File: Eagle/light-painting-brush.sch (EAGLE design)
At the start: 24 parts, among them IC1 TPS61070DDC, T1 2N3904, T2 2N3904, T3 2N3904

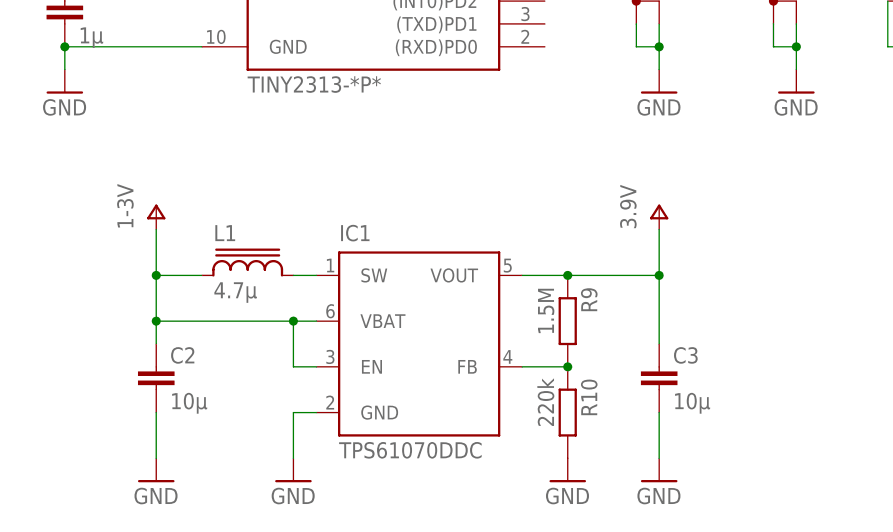
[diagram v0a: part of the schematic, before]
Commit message: Remove TPS61070 boost converter
Previous version of the board is saved in the "tps61070" branch.
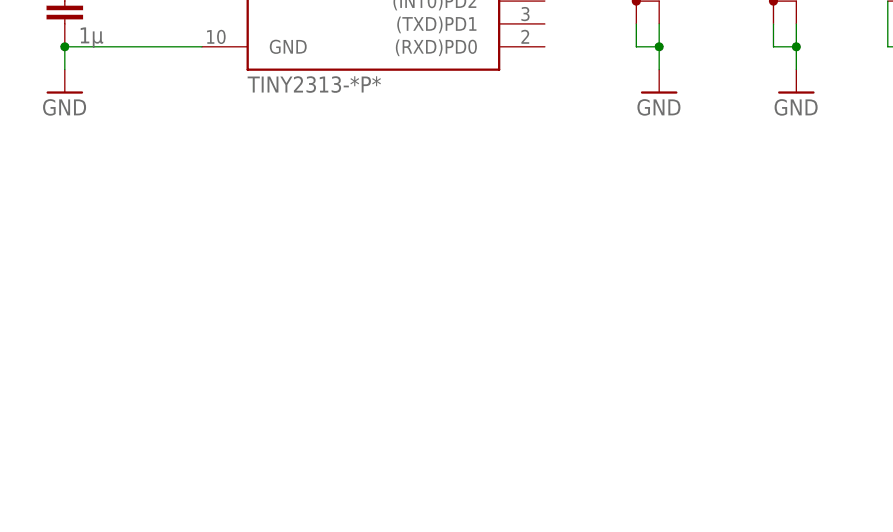
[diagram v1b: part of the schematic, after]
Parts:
- removed C2, C3: 10μ, rcl:C-EUC1206
- removed IC1: TPS61070DDC, Gumix:TPS61070DDC
- removed L1: 4.7μ, inductor-sumida:CR43
- removed R10: 220k, resistor:R-EU_R1206
- removed R9: 1.5M, resistor:R-EU_R1206
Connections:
- removed net N$13: IC1.SW, L1.2
- removed net N$14: IC1.FB, R10.1, R9.2
- net GND: no longer C2.2, C3.2, IC1.GND, R10.2
- net V+: no longer C2.1, C3.1, IC1.EN, IC1.VBAT, IC1.VOUT, L1.1, R9.1
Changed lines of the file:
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@@
 <part name="R2" library="resistor" deviceset="R-EU_" device="R1206" value="10k"/>
 <part name="R3" library="resistor" deviceset="R-EU_" device="R1206" value="10k"/>
-<part name="3V" library="supply1" deviceset="V+" device="" value="1-3V"/>
 <part name="4V" library="supply1" deviceset="V+" device="" value="3.9V"/>
 <part name="T1" library="transistor" deviceset="2N3904" device=""/>
@@
 <part name="4V2" library="supply1" deviceset="V+" device="" value="3.9V"/>
 <part name="4V3" library="supply1" deviceset="V+" device="" value="3.9V"/>
-<part name="L1" library="inductor-sumida" deviceset="CR43" device="" value="4.7μ"/>
-<part name="GND2" library="supply1" deviceset="GND" device=""/>
-<part name="IC1" library="Gumix" deviceset="TPS6107*" device="DDC" technology="0"/>
-<part name="4V4" library="supply1" deviceset="V+" device="" value="3.9V"/>
-<part name="R9" library="resistor" deviceset="R-EU_" device="R1206" value="1.5M"/>
-<part name="R10" library="resistor" deviceset="R-EU_" device="R1206" value="220k"/>
-<part name="GND5" library="supply1" deviceset="GND" device=""/>
-<part name="C2" library="rcl" deviceset="C-EU" device="C1206" value="10μ"/>
-<part name="C3" library="rcl" deviceset="C-EU" device="C1206" value="10μ"/>
-<part name="GND6" library="supply1" deviceset="GND" device=""/>
-<part name="GND7" library="supply1" deviceset="GND" device=""/>
 <part name="GND8" library="supply1" deviceset="GND" device=""/>
 <part name="GND9" library="supply1" deviceset="GND" device=""/>
@@
 <attribute name="VALUE" x="29.718" y="59.69" size="1.778" layer="96" rot="R270"/>
 </instance>
-<instance part="3V" gate="1" x="-38.1" y="-5.08" smashed="yes">
-<attribute name="VALUE" x="-40.64" y="-7.62" size="1.778" layer="96" rot="R90"/>
-</instance>
 <instance part="4V" gate="1" x="-48.26" y="66.04" smashed="yes">
 <attribute name="VALUE" x="-50.8" y="63.5" size="1.778" layer="96" rot="R90"/>
@@
 <instance part="4V3" gate="1" x="86.36" y="66.04" smashed="yes">
 <attribute name="VALUE" x="83.82" y="63.5" size="1.778" layer="96" rot="R90"/>
-</instance>
-<instance part="L1" gate="G$1" x="-27.94" y="-12.7" smashed="yes">
-<attribute name="NAME" x="-31.75" y="-8.89" size="1.778" layer="95"/>
-<attribute name="VALUE" x="-31.75" y="-15.24" size="1.778" layer="96"/>
-</instance>
-<instance part="GND2" gate="1" x="-38.1" y="-35.56" smashed="yes">
-<attribute name="VALUE" x="-40.64" y="-38.1" size="1.778" layer="96"/>
-</instance>
-<instance part="IC1" gate="G$1" x="-10.16" y="-20.32" smashed="yes">
-<attribute name="NAME" x="-17.78" y="-8.89" size="1.778" layer="95"/>
-<attribute name="VALUE" x="-17.78" y="-33.02" size="1.778" layer="96"/>
-</instance>
-<instance part="4V4" gate="1" x="17.78" y="-5.08" smashed="yes">
-<attribute name="VALUE" x="15.24" y="-7.62" size="1.778" layer="96" rot="R90"/>
-</instance>
-<instance part="R9" gate="G$1" x="7.62" y="-17.78" smashed="yes" rot="R270">
-<attribute name="NAME" x="9.1186" y="-13.97" size="1.778" layer="95" rot="R270"/>
-<attribute name="VALUE" x="4.318" y="-13.97" size="1.778" layer="96" rot="R270"/>
-</instance>
-<instance part="R10" gate="G$1" x="7.62" y="-27.94" smashed="yes" rot="R270">
-<attribute name="NAME" x="9.1186" y="-24.13" size="1.778" layer="95" rot="R270"/>
-<attribute name="VALUE" x="4.318" y="-24.13" size="1.778" layer="96" rot="R270"/>
-</instance>
-<instance part="GND5" gate="1" x="7.62" y="-35.56" smashed="yes">
-<attribute name="VALUE" x="5.08" y="-38.1" size="1.778" layer="96"/>
-</instance>
-<instance part="C2" gate="G$1" x="-38.1" y="-22.86" smashed="yes">
-<attribute name="NAME" x="-36.576" y="-22.479" size="1.778" layer="95"/>
-<attribute name="VALUE" x="-36.576" y="-27.559" size="1.778" layer="96"/>
-</instance>
-<instance part="C3" gate="G$1" x="17.78" y="-22.86" smashed="yes">
-<attribute name="NAME" x="19.304" y="-22.479" size="1.778" layer="95"/>
-<attribute name="VALUE" x="19.304" y="-27.559" size="1.778" layer="96"/>
-</instance>
-<instance part="GND6" gate="1" x="-22.86" y="-35.56" smashed="yes">
-<attribute name="VALUE" x="-25.4" y="-38.1" size="1.778" layer="96"/>
-</instance>
-<instance part="GND7" gate="1" x="17.78" y="-35.56" smashed="yes">
-<attribute name="VALUE" x="15.24" y="-38.1" size="1.778" layer="96"/>
 </instance>
 <instance part="GND8" gate="1" x="17.78" y="7.62" smashed="yes">
@@
 <pinref part="GND3" gate="1" pin="GND"/>
 <wire x1="50.8" y1="0" x2="50.8" y2="-2.54" width="0.1524" layer="91"/>
-</segment>
-<segment>
-<pinref part="R10" gate="G$1" pin="2"/>
-<pinref part="GND5" gate="1" pin="GND"/>
-</segment>
-<segment>
-<pinref part="GND6" gate="1" pin="GND"/>
-<wire x1="-22.86" y1="-33.02" x2="-22.86" y2="-27.94" width="0.1524" layer="91"/>
-<pinref part="IC1" gate="G$1" pin="GND"/>
-<wire x1="-22.86" y1="-27.94" x2="-20.32" y2="-27.94" width="0.1524" layer="91"/>
-</segment>
-<segment>
-<pinref part="C2" gate="G$1" pin="2"/>
-<pinref part="GND2" gate="1" pin="GND"/>
-<wire x1="-38.1" y1="-27.94" x2="-38.1" y2="-33.02" width="0.1524" layer="91"/>
-</segment>
-<segment>
-<pinref part="GND7" gate="1" pin="GND"/>
-<pinref part="C3" gate="G$1" pin="2"/>
-<wire x1="17.78" y1="-33.02" x2="17.78" y2="-27.94" width="0.1524" layer="91"/>
 </segment>
 <segment>
@@
 </segment>
 <segment>
-<pinref part="3V" gate="1" pin="V+"/>
-<wire x1="-38.1" y1="-7.62" x2="-38.1" y2="-12.7" width="0.1524" layer="91"/>
-<pinref part="L1" gate="G$1" pin="1"/>
-<wire x1="-38.1" y1="-12.7" x2="-33.02" y2="-12.7" width="0.1524" layer="91"/>
-<wire x1="-38.1" y1="-20.32" x2="-38.1" y2="-17.78" width="0.1524" layer="91"/>
-<junction x="-38.1" y="-12.7"/>
-<pinref part="C2" gate="G$1" pin="1"/>
-<pinref part="IC1" gate="G$1" pin="VBAT"/>
-<wire x1="-38.1" y1="-17.78" x2="-38.1" y2="-12.7" width="0.1524" layer="91"/>
-<wire x1="-20.32" y1="-17.78" x2="-22.86" y2="-17.78" width="0.1524" layer="91"/>
-<pinref part="IC1" gate="G$1" pin="EN"/>
-<wire x1="-20.32" y1="-22.86" x2="-22.86" y2="-22.86" width="0.1524" layer="91"/>
-<wire x1="-22.86" y1="-22.86" x2="-22.86" y2="-17.78" width="0.1524" layer="91"/>
-<wire x1="-22.86" y1="-17.78" x2="-38.1" y2="-17.78" width="0.1524" layer="91"/>
-<junction x="-38.1" y="-17.78"/>
-<junction x="-22.86" y="-17.78"/>
-</segment>
-<segment>
-<pinref part="IC1" gate="G$1" pin="VOUT"/>
-<wire x1="2.54" y1="-12.7" x2="7.62" y2="-12.7" width="0.1524" layer="91"/>
-<pinref part="R9" gate="G$1" pin="1"/>
-<junction x="7.62" y="-12.7"/>
-<pinref part="4V4" gate="1" pin="V+"/>
-<wire x1="7.62" y1="-12.7" x2="17.78" y2="-12.7" width="0.1524" layer="91"/>
-<wire x1="17.78" y1="-12.7" x2="17.78" y2="-7.62" width="0.1524" layer="91"/>
-<pinref part="C3" gate="G$1" pin="1"/>
-<wire x1="17.78" y1="-20.32" x2="17.78" y2="-12.7" width="0.1524" layer="91"/>
-<junction x="17.78" y="-12.7"/>
-</segment>
-<segment>
 <pinref part="R2" gate="G$1" pin="1"/>
 <pinref part="4V5" gate="1" pin="V+"/>
@@
 </segment>
 </net>
-<net name="N$13" class="0">
-<segment>
-<pinref part="L1" gate="G$1" pin="2"/>
-<wire x1="-20.32" y1="-12.7" x2="-22.86" y2="-12.7" width="0.1524" layer="91"/>
-<pinref part="IC1" gate="G$1" pin="SW"/>
-</segment>
-</net>
-<net name="N$14" class="0">
-<segment>
-<pinref part="R9" gate="G$1" pin="2"/>
-<pinref part="R10" gate="G$1" pin="1"/>
-<pinref part="IC1" gate="G$1" pin="FB"/>
-<wire x1="2.54" y1="-22.86" x2="7.62" y2="-22.86" width="0.1524" layer="91"/>
-<junction x="7.62" y="-22.86"/>
-</segment>
-</net>

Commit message: Redesign the PCB assuming 4V input
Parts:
- removed LSP1, LSP2: LSP10, solpad:LSP10
- added 4V_PAD, GND_PAD: LSP10, solpad:LSP10
- R8: value 100 -> 90
- renumbered S1 to BTN1, S2 to BTN2, U$1 to AVR
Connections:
- net N$10 renamed BLUE0
- net N$2 renamed RED
- net N$3 renamed GREEN
- net N$4 renamed BLUE
- net N$8 renamed RED0
- net N$9 renamed GREEN0
- removed net V+: AVR.VCC, C1.1, LSP1.MP, R1.1, R2.1, R3.1, R7.1, R8.1, T3.C
- new net VCC: 4V_PAD.MP, AVR.VCC, C1.1, R1.1, R2.1, R3.1, R7.1, R8.1, T3.C
- net GND: now also GND_PAD.MP; no longer LSP2.MP
- net N$15: now also BTN1.2.2
- net N$16: now also BTN2.2.1

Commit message: Move C1 closer to VCC and GND pins of AVR
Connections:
- net N$11 renamed RED2
- net N$12 renamed GREEN2
- net N$5 renamed RED1
- net N$6 renamed GREEN1
- net N$7 renamed BLUE1
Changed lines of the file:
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@@
 </segment>
 </net>
-<net name="N$5" class="0">
+<net name="RED1" class="0">
 <segment>
 <pinref part="R4" gate="G$1" pin="2"/>
@@
 </segment>
 </net>
-<net name="N$6" class="0">
+<net name="GREEN1" class="0">
 <segment>
 <pinref part="R5" gate="G$1" pin="2"/>
@@
 </segment>
 </net>
-<net name="N$7" class="0">
+<net name="BLUE1" class="0">
 <segment>
 <pinref part="R6" gate="G$1" pin="2"/>
@@
 </segment>
 </net>
-<net name="N$11" class="0">
+<net name="RED2" class="0">
 <segment>
 <pinref part="T1" gate="G1" pin="C"/>
@@
 </segment>
 </net>
-<net name="N$12" class="0">
+<net name="GREEN2" class="0">
 <segment>
 <pinref part="T2" gate="G1" pin="C"/>

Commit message: Update values assuming 5V input
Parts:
- R6: value 5.6k -> 10k
- R8: value 90 -> 100
- renumbered 4V_PAD to 5V_PAD
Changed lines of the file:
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@@
 <part name="T2" library="transistor" deviceset="2N3904" device=""/>
 <part name="T3" library="transistor" deviceset="2N3904" device=""/>
-<part name="R6" library="resistor" deviceset="R-EU_" device="R1206" value="5.6k"/>
+<part name="R6" library="resistor" deviceset="R-EU_" device="R1206" value="10k"/>
 <part name="GND3" library="supply1" deviceset="GND" device=""/>
 <part name="GND4" library="supply1" deviceset="GND" device=""/>
@@
 <part name="D1" library="Gumix" deviceset="LED-RGB-CC-THRU" device="DIFFUSE"/>
 <part name="R7" library="resistor" deviceset="R-EU_" device="R1206" value="100"/>
-<part name="R8" library="resistor" deviceset="R-EU_" device="R1206" value="90"/>
+<part name="R8" library="resistor" deviceset="R-EU_" device="R1206" value="100"/>
 <part name="GND8" library="supply1" deviceset="GND" device=""/>
 <part name="GND9" library="supply1" deviceset="GND" device=""/>
-<part name="4V_PAD" library="solpad" deviceset="LSP10" device=""/>
+<part name="5V_PAD" library="solpad" deviceset="LSP10" device=""/>
 <part name="GND_PAD" library="solpad" deviceset="LSP10" device=""/>
 <part name="GND10" library="supply1" deviceset="GND" device=""/>
@@
 <attribute name="VALUE" x="30.48" y="5.08" size="1.778" layer="96"/>
 </instance>
-<instance part="4V_PAD" gate="1" x="-27.94" y="-2.54" smashed="yes">
+<instance part="5V_PAD" gate="1" x="-27.94" y="-2.54" smashed="yes">
 <attribute name="NAME" x="-29.21" y="0.381" size="1.778" layer="95"/>
 </instance>
@@
 <segment>
 <wire x1="-33.02" y1="-2.54" x2="-33.02" y2="-10.16" width="0.1524" layer="91"/>
-<pinref part="4V_PAD" gate="1" pin="MP"/>
+<pinref part="5V_PAD" gate="1" pin="MP"/>
 <wire x1="-27.94" y1="-10.16" x2="-27.94" y2="-5.08" width="0.1524" layer="91"/>
 <wire x1="-33.02" y1="-10.16" x2="-27.94" y2="-10.16" width="0.1524" layer="91"/>
